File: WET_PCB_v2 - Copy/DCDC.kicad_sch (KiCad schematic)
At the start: 8 parts, among them Q5 Q_NMOS_GDS, Q6 Q_NMOS_GDS

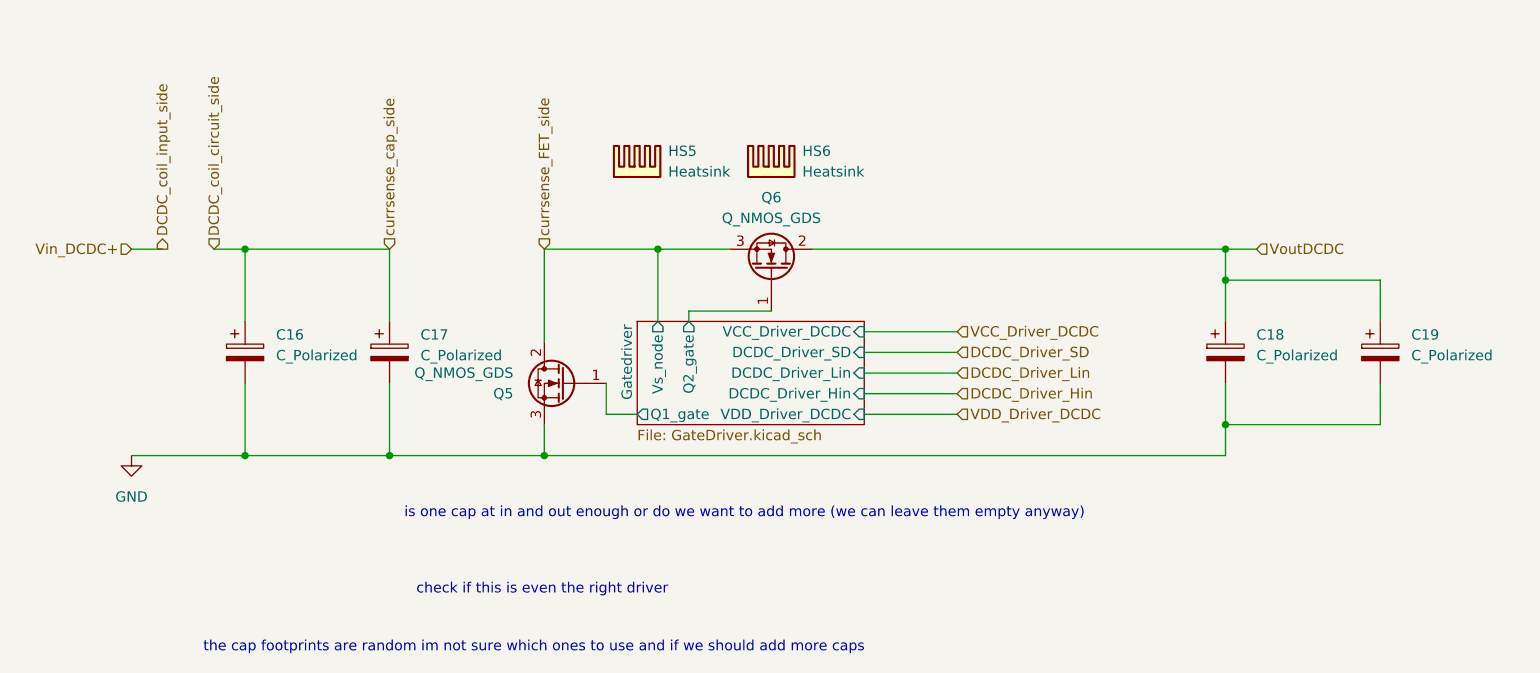
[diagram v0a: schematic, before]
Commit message: microcontroller to chip traces done
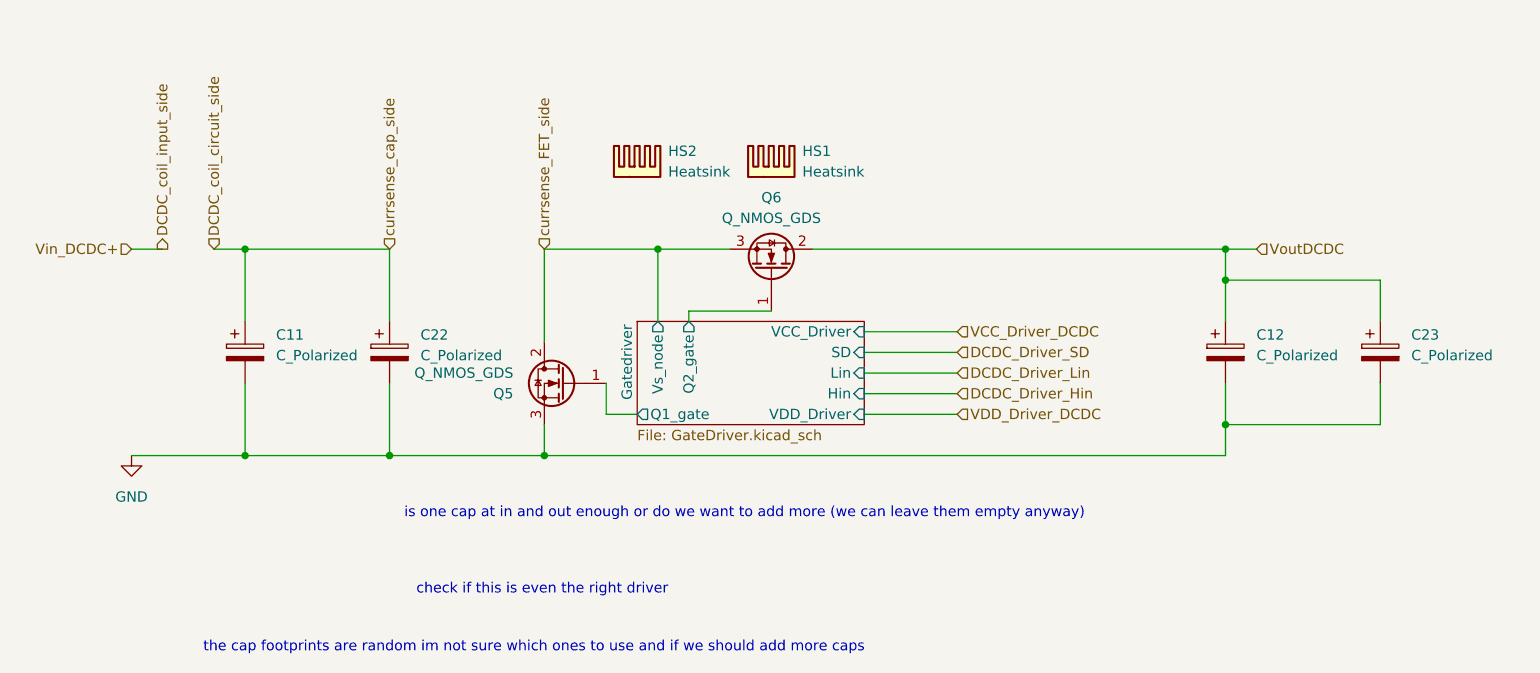
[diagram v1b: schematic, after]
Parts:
- renumbered C16 to C11, C18 to C12, C17 to C22, C19 to C23, HS6 to HS1, HS5 to HS2
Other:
- sheet Gatedriver ports: added Hin, Lin, SD, VCC_Driver, VDD_Driver; removed DCDC_Driver_Hin, DCDC_Driver_Lin, DCDC_Driver_SD, VCC_Driver_DCDC, VDD_Driver_DCDC
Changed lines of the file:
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@@
 		(dnp no)
 		(fields_autoplaced yes)
-		(property "Reference" "C18"
+		(property "Reference" "C12"
 			(at 179.07 53.7209 0)
 			(show_name no)
@@
 			(project "WET_PCB_v2"
 				(path "/13451c35-1666-47d9-9525-8d8125ba1cf3/04007180-46fe-4cf0-9e6f-a7d321798318"
-					(reference "C18")
+					(reference "C12")
 					(unit 1)
 				)
@@
 		(dnp no)
 		(fields_autoplaced yes)
-		(property "Reference" "HS6"
+		(property "Reference" "HS1"
 			(at 123.19 31.1149 0)
 			(show_name no)
@@
 			(project "WET_PCB_v2"
 				(path "/13451c35-1666-47d9-9525-8d8125ba1cf3/04007180-46fe-4cf0-9e6f-a7d321798318"
-					(reference "HS6")
+					(reference "HS1")
 					(unit 1)
 				)
@@
 		(dnp no)
 		(fields_autoplaced yes)
-		(property "Reference" "C19"
+		(property "Reference" "C23"
 			(at 198.12 53.7209 0)
 			(show_name no)
@@
 			(project "WET_PCB_v2"
 				(path "/13451c35-1666-47d9-9525-8d8125ba1cf3/04007180-46fe-4cf0-9e6f-a7d321798318"
-					(reference "C19")
+					(reference "C23")
 					(unit 1)
 				)
@@
 		(dnp no)
 		(fields_autoplaced yes)
-		(property "Reference" "#PWR044"
+		(property "Reference" "#PWR04"
 			(at 40.64 74.93 0)
 			(hide yes)
@@
 			(project "WET_PCB_v2"
 				(path "/13451c35-1666-47d9-9525-8d8125ba1cf3/04007180-46fe-4cf0-9e6f-a7d321798318"
-					(reference "#PWR044")
+					(reference "#PWR04")
 					(unit 1)
 				)
@@
 		(dnp no)
 		(fields_autoplaced yes)
-		(property "Reference" "C17"
+		(property "Reference" "C22"
 			(at 76.2 53.7209 0)
 			(show_name no)
@@
 			(project "WET_PCB_v2"
 				(path "/13451c35-1666-47d9-9525-8d8125ba1cf3/04007180-46fe-4cf0-9e6f-a7d321798318"
-					(reference "C17")
+					(reference "C22")
 					(unit 1)
 				)
@@
 		(dnp no)
 		(fields_autoplaced yes)
-		(property "Reference" "C16"
+		(property "Reference" "C11"
 			(at 58.42 53.7209 0)
 			(show_name no)
@@
 			(project "WET_PCB_v2"
 				(path "/13451c35-1666-47d9-9525-8d8125ba1cf3/04007180-46fe-4cf0-9e6f-a7d321798318"
-					(reference "C16")
+					(reference "C11")
 					(unit 1)
 				)
@@
 		(dnp no)
 		(fields_autoplaced yes)
-		(property "Reference" "HS5"
+		(property "Reference" "HS2"
 			(at 106.68 31.1149 0)
 			(show_name no)
@@
 			(project "WET_PCB_v2"
 				(path "/13451c35-1666-47d9-9525-8d8125ba1cf3/04007180-46fe-4cf0-9e6f-a7d321798318"
-					(reference "HS5")
+					(reference "HS2")
 					(unit 1)
 				)
@@
 			)
 		)
-		(pin "DCDC_Driver_Hin" input
+		(pin "Hin" input
 			(at 130.81 60.96 0)
 			(effects
@@
 			)
 		)
-		(pin "DCDC_Driver_Lin" input
+		(pin "Lin" input
 			(at 130.81 58.42 0)
 			(effects
@@
 			)
 		)
-		(pin "DCDC_Driver_SD" input
+		(pin "SD" input
 			(at 130.81 55.88 0)
 			(effects
@@
 			)
 		)
-		(pin "VCC_Driver_DCDC" input
+		(pin "VCC_Driver" input
 			(at 130.81 53.34 0)
 			(effects
@@
 			)
 		)
-		(pin "VDD_Driver_DCDC" input
+		(pin "VDD_Driver" input
 			(at 130.81 63.5 0)
 			(effects
